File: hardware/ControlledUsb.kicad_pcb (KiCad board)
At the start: 4 copper layers, 62 x 20 mm, 31 parts, among them J1 USB_A_Male, J2 USB_A_Female, SW1 USER_BTN, U1 RP2040, U2 W25Q32, U3 CH334F, U4 TPS22918, U5 CH440P, U6 ME6211C33, U7 USBLC6-2SC6, Y1 12.000MHz, Y2 12.000MHz

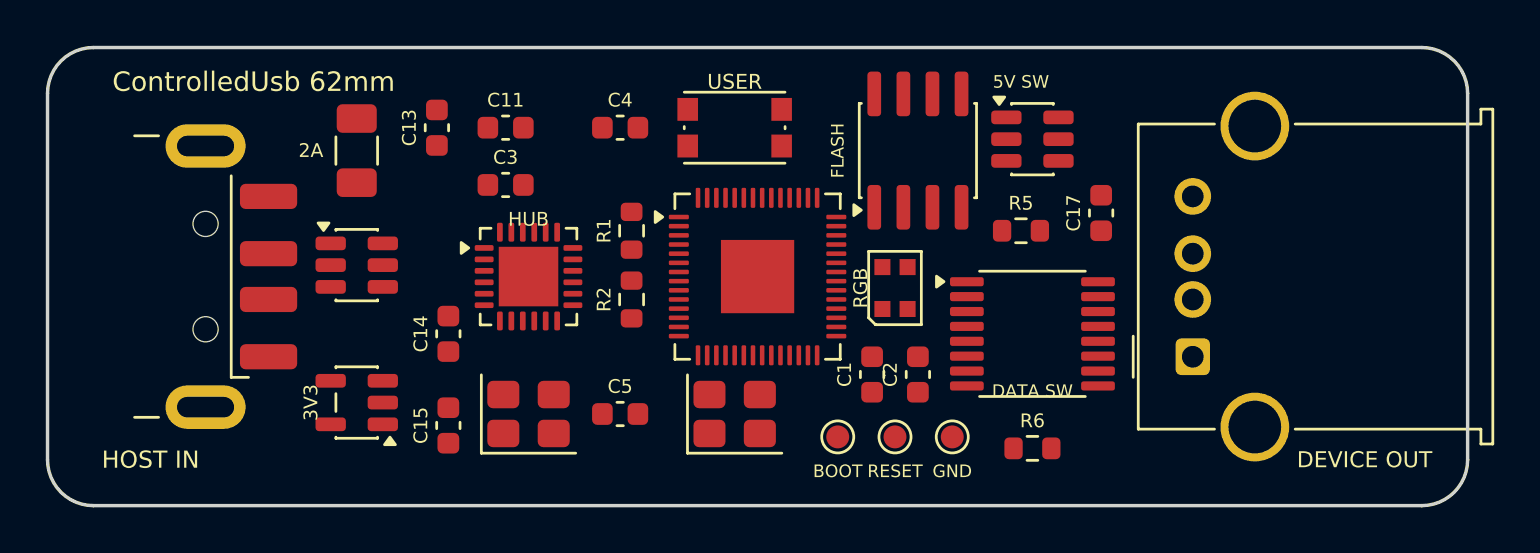
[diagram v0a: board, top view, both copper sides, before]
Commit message: Auto-route the board using freerouting
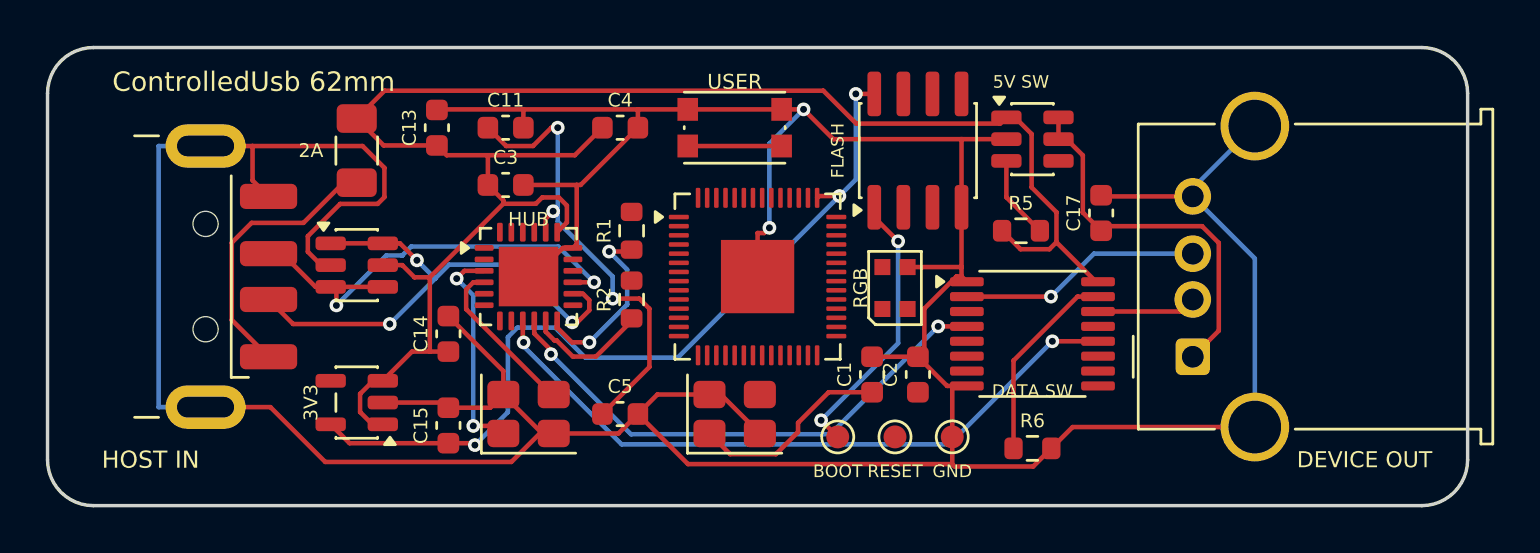
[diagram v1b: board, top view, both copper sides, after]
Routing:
- net GND: track 0.00 -> 188.8 mm, vias 0 -> 2
- net +5V_FUSED: track 0.00 -> 76.9 mm
- net +3V3: track 0.00 -> 36.7 mm, vias 0 -> 3
- net HUB_PORT2_DM: track 0.00 -> 29.8 mm, vias 0 -> 2
- net HUB_PORT2_DP: track 0.00 -> 23.3 mm, vias 0 -> 2
- net USB_HOST_DM: track 0.00 -> 23.3 mm, vias 0 -> 3
- net HUB_V33: track 0.00 -> 20.7 mm, vias 0 -> 3
- net USB_HOST_DP: track 0.00 -> 20.3 mm, vias 0 -> 2
- net VBUS_SW: track 0.00 -> 16.9 mm
- net +5V: track 0.00 -> 12.2 mm
- net QSPI_SS: track 0.00 -> 12.1 mm, vias 0 -> 2
- net SW_DP: track 0.00 -> 10.6 mm, vias 0 -> 1
- net HUB_XI: track 0.00 -> 9.52 mm, vias 0 -> 2
- net MCU_XI: track 0.00 -> 8.83 mm
- net DATA_OE_N: track 0.00 -> 8.68 mm
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
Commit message: Complete 100% routing with 0 DRC violations, 0.00mm skew USB differential pairs, and manufacturing deliverables
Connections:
- U7 pad 1: USB_HOST_DM -> USB_HOST_DP
- U7 pad 3: USB_HOST_DP -> USB_HOST_DM
- U7 pad 4: USB_HOST_DP -> USB_HOST_DM
- U7 pad 6: USB_HOST_DM -> USB_HOST_DP
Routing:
- net MCU_XO: track 0.00 -> 23.4 mm
- net GND: track 188.8 -> 206.1 mm
- net +3V3: track 36.7 -> 53.3 mm, vias 3 -> 5
- net QSPI_SCLK: track 0.00 -> 16.6 mm
- net PWR_EN: track 3.66 -> 17.5 mm, vias 0 -> 2
- net QSPI_SD0: track 0.00 -> 13.5 mm, vias 0 -> 2
- net QSPI_SD2: track 0.00 -> 12.6 mm, vias 0 -> 2
- net USER_BTN: track 4.10 -> 16.7 mm
- net HUB_PORT2_DM: track 29.8 -> 42.1 mm, vias 2 -> 0
- net +5V_FUSED: track 76.9 -> 64.9 mm, vias 0 -> 3
- net MCU_USB_DM: track 0.00 -> 10.8 mm, vias 0 -> 2
- net +1V1: track 0.00 -> 10.5 mm
- net QSPI_SD1: track 0.00 -> 10.4 mm
- net DATA_OE_N: track 8.68 -> 19.0 mm, vias 0 -> 2
- net MCU_XI: track 8.83 -> 19.0 mm
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- added copper zone on B.Cu, net GND
- added copper zone on In1.Cu, net GND
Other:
- board text removed: "3V3"
- board text removed: "DATA SW"
- board text removed: "HUB"
- board text removed: "RGB"
